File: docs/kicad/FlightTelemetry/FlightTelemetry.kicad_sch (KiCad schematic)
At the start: 4 parts, among them J1 BMP388, J2 NEO-M9N, J3 Micro SD, U1 ESP32 DevKitC V4

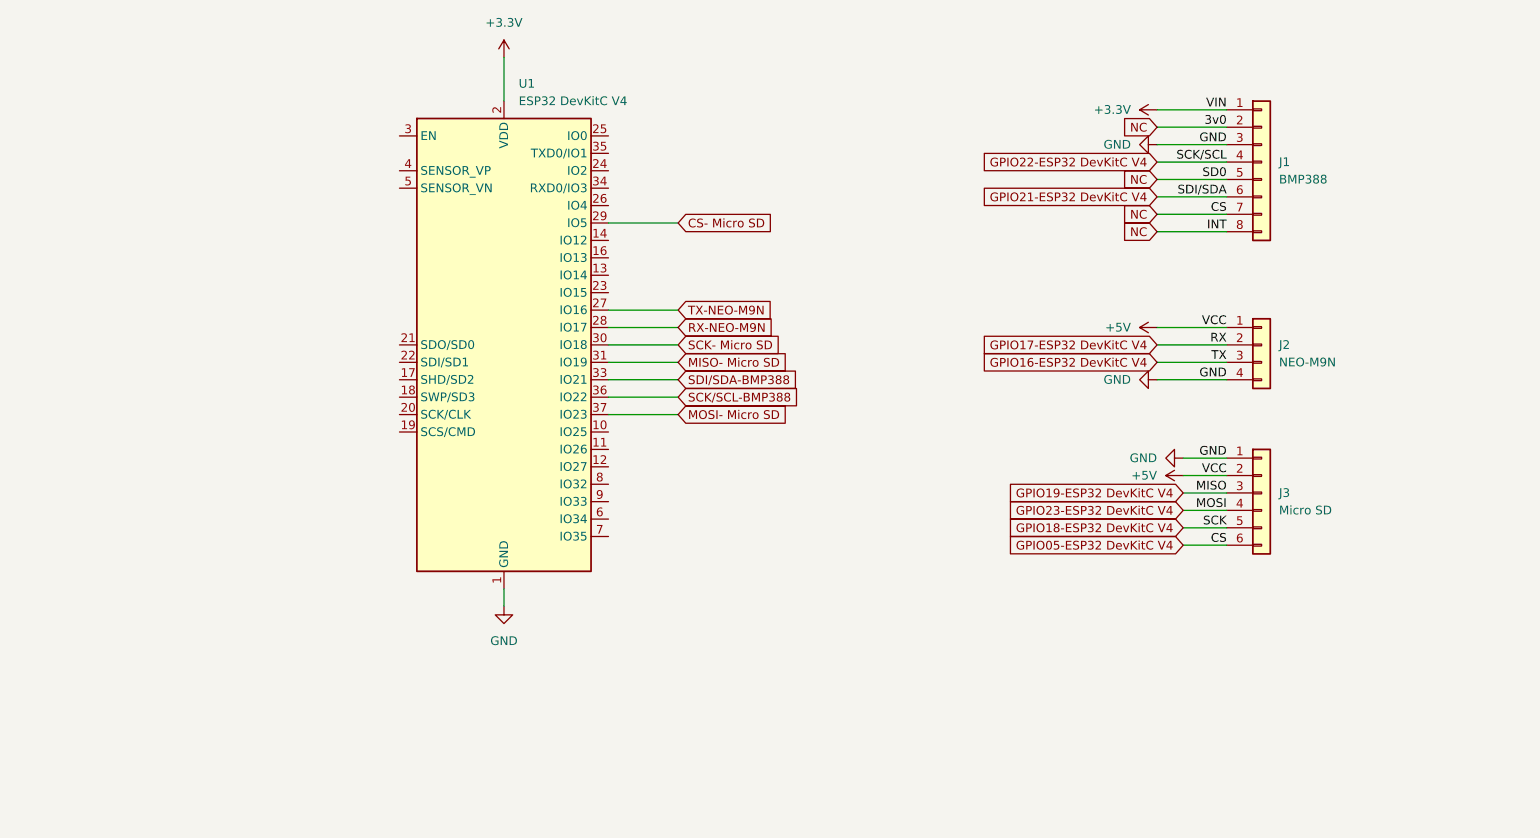
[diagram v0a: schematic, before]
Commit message: Docs: add INA219 power monitoring and battery architecture4
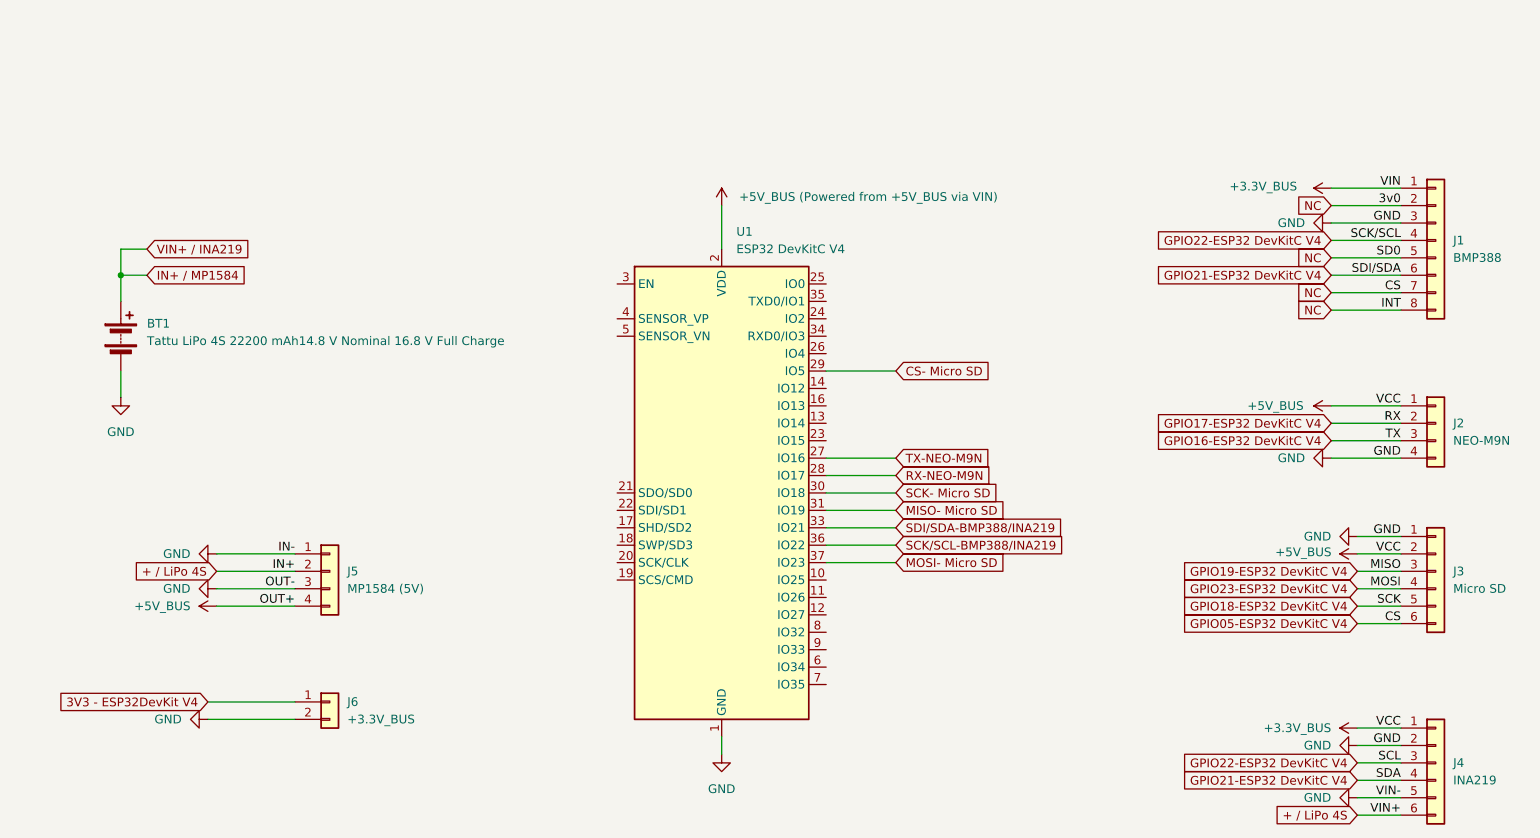
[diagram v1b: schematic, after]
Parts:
- added BT1: Tattu LiPo 4S 22200 mAh14.8 V Nominal 16.8 V Full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, symbol Device:Battery
- added J4: INA219, symbol Connector_Generic:Conn_01x06
- added J5: MP1584 (5V), symbol Connector_Generic:Conn_01x04
- added J6: +3.3V_BUS, symbol Connector_Generic:Conn_01x02
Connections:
- net +5V is gone; now on net +3.3V_BUS: J2.1 (Pin_1), J3.2 (Pin_2)
- net GND: now also BT1.2 (-), J4.2 (Pin_2), J4.5 (Pin_5), J5.1 (Pin_1), J5.3 (Pin_3), J6.2 (Pin_2)
- net GPIO21-ESP32 DevKitC V4: now also J4.4 (Pin_4)
- net GPIO22-ESP32 DevKitC V4: now also J4.3 (Pin_3)
- net +3.3V renamed +3.3V_BUS
- net +3.3V_BUS: now also J4.1 (Pin_1), J5.4 (Pin_4); no longer U1.2 (VDD)
- net SCK/SCL-BMP388 renamed SCK/SCL-BMP388/INA219
- net SDI/SDA-BMP388 renamed SDI/SDA-BMP388/INA219
- new net + / LiPo 4S: J4.6 (Pin_6), J5.2 (Pin_2)
- new net +5V_BUS (Powered from +5V_BUS via VIN): U1.2 (VDD)
- new net 3V3 - ESP32DevKit V4: J6.1 (Pin_1)
- new net IN+ / MP1584: BT1.1 (+)
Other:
- moved on the sheet: J1, J2, J3, U1

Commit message: Docs: add Sprint 9 power architecture and real hardware prototype
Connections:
- net + / LiPo 4S: no longer J5.2 (Pin_2)
- net GND: no longer J4.5 (Pin_5)
- net IN+ / MP1584: now also J4.5 (Pin_5)
- new net VIN- / INA219: J5.2 (Pin_2)
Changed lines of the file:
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@@
+		)
+	)
+	(global_label "IN+ {slash} MP1584"
+		(shape input)
+		(at 214.63 130.81 180)
+		(fields_autoplaced yes)
+		(effects
+			(font
+				(size 1.27 1.27)
+			)
+			(justify right)
+		)
+		(property "Intersheetrefs" "${INTERSHEET_REFS}"
+			(at 197.312 130.81 0)
+			(hide yes)
+			(show_name no)
+			(do_not_autoplace no)
+			(effects
+				(font
+					(size 1.27 1.27)
+				)
+				(justify right)
+			)
 		)
 	)
@@
 		)
 	)
-	(global_label "+ {slash} LiPo 4S"
+	(global_label "VIN- {slash} INA219"
 		(shape input)
 		(at 48.26 97.79 180)
@@
 		)
 		(property "Intersheetrefs" "${INTERSHEET_REFS}"
-			(at 32.9982 97.79 0)
+			(at 30.7604 97.79 0)
 			(hide yes)
 			(show_name no)
@@
 					(unit 1)
 				)
-			)
-		)
-	)
-	(symbol
-		(lib_id "power:GND")
-		(at 214.63 130.81 270)
-		(unit 1)
-		(body_style 1)
-		(exclude_from_sim no)
-		(in_bom yes)
-		(on_board yes)
-		(in_pos_files yes)
-		(dnp no)
-		(fields_autoplaced yes)
-		(property "Reference" "#PWR013"
-			(at 208.28 130.81 0)
-			(hide yes)
-			(show_name no)
-			(do_not_autoplace no)
-			(effects
-				(font
-					(size 1.27 1.27)
-				)
-			)
-		)
-		(property "Value" "GND"
-			(at 210.82 130.8099 90)
-			(show_name no)
-			(do_not_autoplace no)
-			(effects
-				(font
-					(size 1.27 1.27)
-				)
-				(justify right)
-			)
-		)
-		(property "Footprint" ""
-			(at 214.63 130.81 0)
-			(hide yes)
-			(show_name no)
-			(do_not_autoplace no)
-			(effects
-				(font
-					(size 1.27 1.27)
-				)
-			)
-		)
-		(property "Datasheet" ""
-			(at 214.63 130.81 0)
-			(hide yes)
-			(show_name no)
-			(do_not_autoplace no)
-			(effects
-				(font
-					(size 1.27 1.27)
-				)
-			)
-		)
-		(property "Description" "Power symbol creates a global label with name \"GND\" , ground"
-			(at 214.63 130.81 0)
-			(hide yes)
-			(show_name no)
-			(do_not_autoplace no)
-			(effects
-				(font
-					(size 1.27 1.27)
-				)
-			)
-		)
-		(pin "1"
-		)
-		(instances
-			(project "FlightTelemetry"
-				(path "/e31ac7f1-555d-4190-a97f-833d688a3009"
-					(reference "#PWR013")
-					(unit 1)
-				)
